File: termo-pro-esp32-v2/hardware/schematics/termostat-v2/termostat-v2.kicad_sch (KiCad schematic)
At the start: 21 parts, among them J1 Conn_01x08_Pin, Q1 PN2222A, Q2 PN2222A, SW1 SW_Push, SW2 SW_Push, SW3 SW_Push, SW4 SW_Push, U1 NODEMCU-32S, U2 DHT11

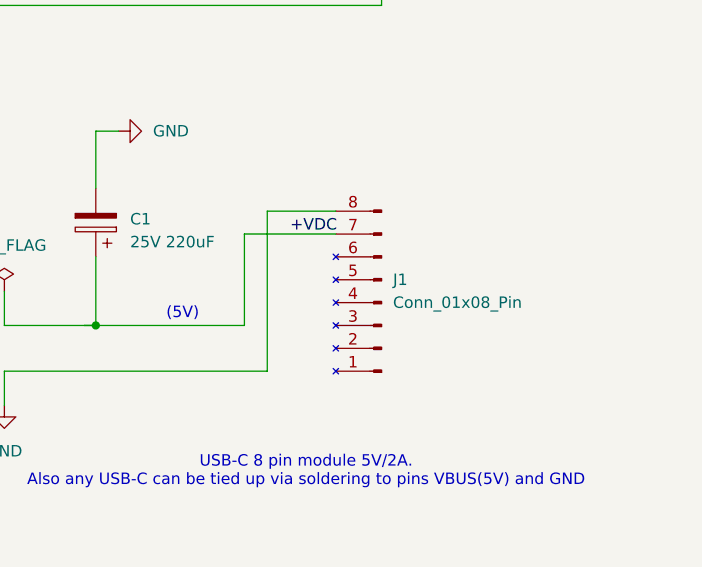
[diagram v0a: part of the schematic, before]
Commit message: Starting Unit PCB compleate.
Some footprint issues were encountered on the initial unit PCB, regarding the ceramic capacitors and the 1×02 5.08 mm screw terminal.

-In the thermostat schematic, the ceramic capacitors were updated to a disc footprint , as well in the starting unit scheme.

-Thermostat PCB is currently in progress.
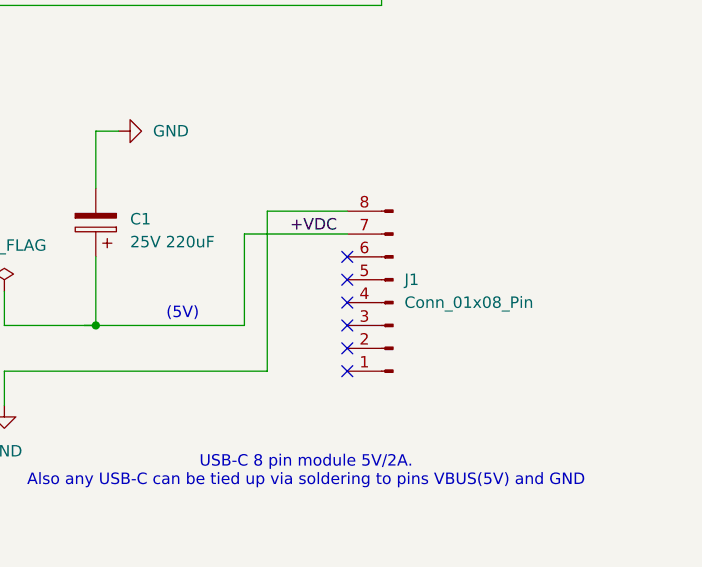
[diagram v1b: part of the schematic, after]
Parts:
- C2, C3, C4: footprint Capacitor_THT:C_Radial_D10.0mm_H12.5mm_P5.00mm -> Capacitor_THT:C_Disc_D11.0mm_W5.0mm_P5.00mm
- J1: footprint Connector_PinHeader_2.54mm:PinHeader_1x08_P2.54mm_Vertical -> Connector_PinSocket_2.54mm:PinSocket_1x08_P2.54mm_Vertical
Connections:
- no-connect marks 17 -> 23
